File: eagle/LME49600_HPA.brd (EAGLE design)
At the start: 93.7 x 71.1 mm, 41 parts, among them IC1 OPA2134P, IC2 OPA2134P

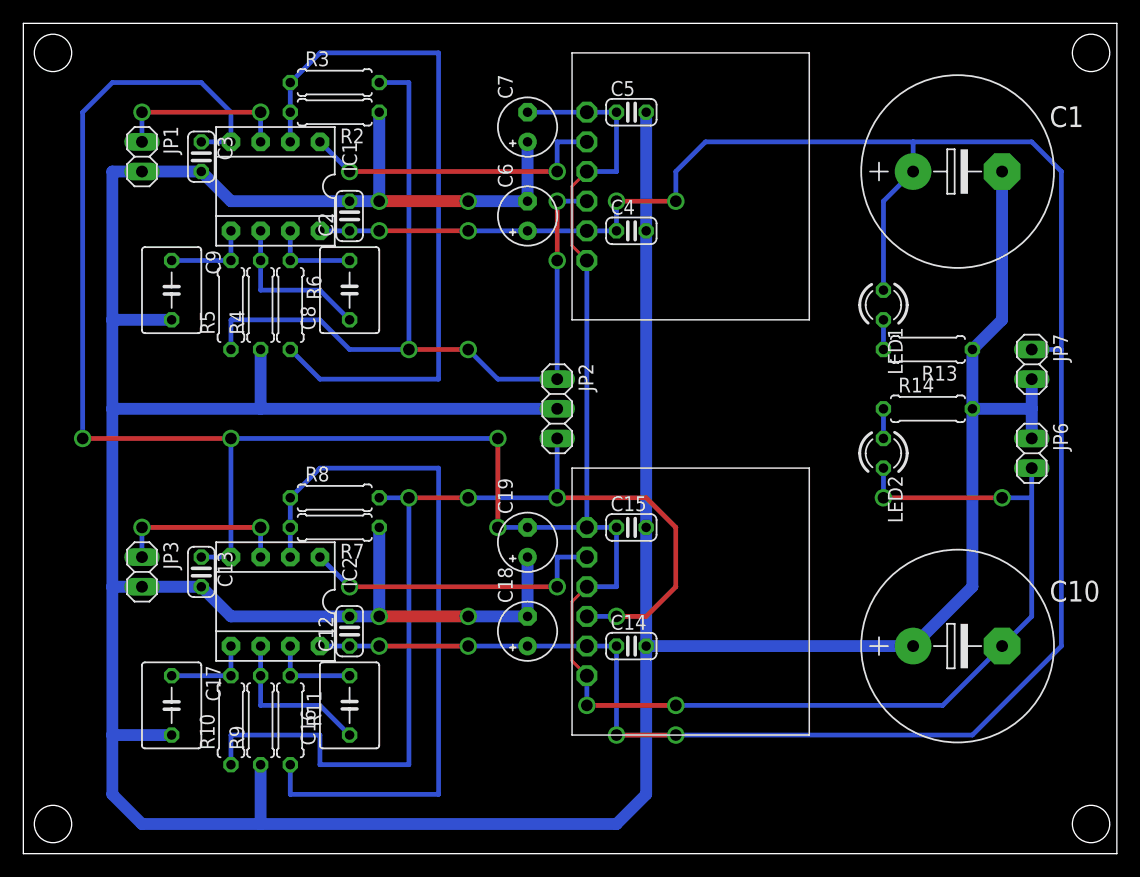
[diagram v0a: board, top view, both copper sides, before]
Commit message: Update: the board design (tantal->Alminium)
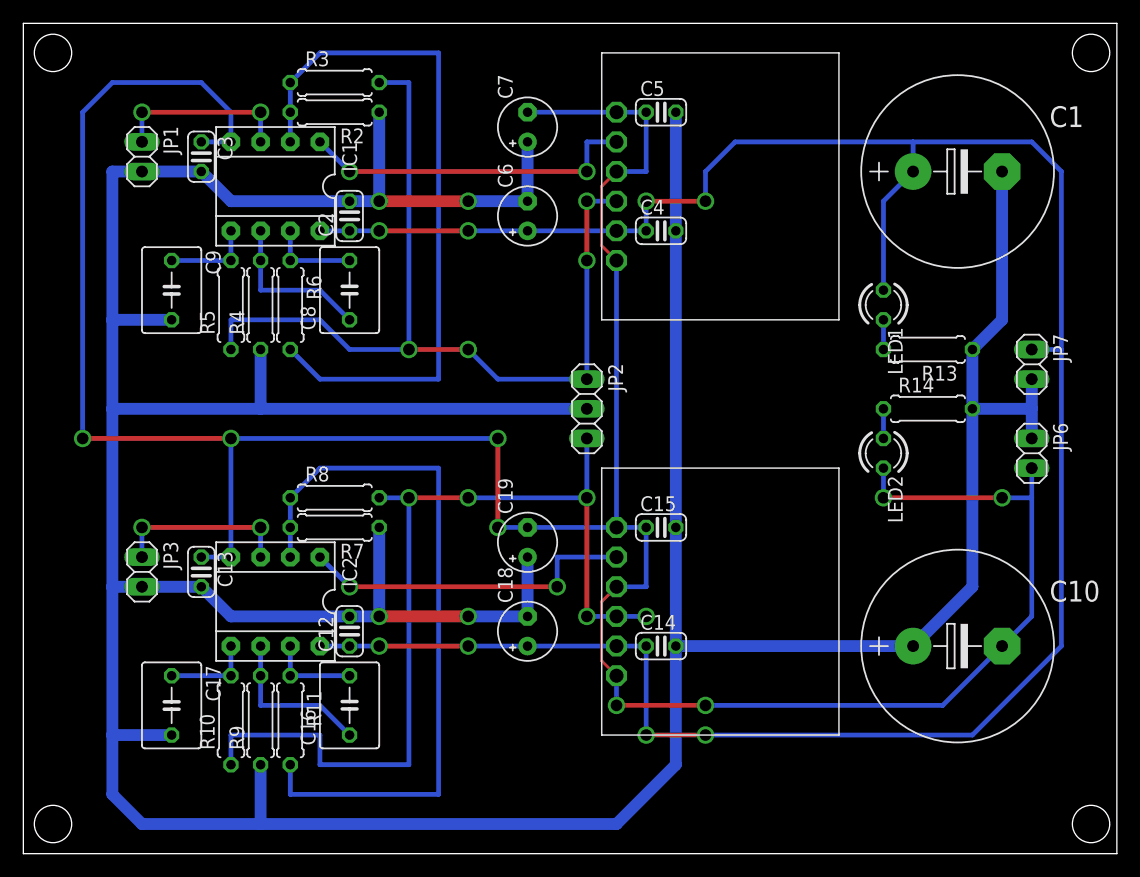
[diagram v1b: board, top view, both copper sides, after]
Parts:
- moved C14 2.54 mm to (54.6, 17.8)
- moved C15 2.54 mm to (54.6, 27.9)
- moved C4 2.54 mm to (54.6, 53.3)
- moved C5 2.54 mm to (54.6, 63.5)
- moved JP2 2.54 mm to (48.3, 38.1)
- moved U$1 2.54 mm to (59.7, 57.1)
- moved U$2 2.54 mm to (59.7, 21.6)
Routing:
- net N$13: track 88.5 -> 81.3 mm, vias 4 -> 5
- net V-: track 248.7 -> 251.2 mm
- net N$7: track 26.5 -> 29.0 mm
- net N$5: track 26.5 -> 29.0 mm
- net N$14: track 75.8 -> 78.3 mm
- net AGND: track 396.0 -> 397.0 mm

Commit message: Update: Eagle files
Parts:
- C18, C19, C6, C7: value 4.7uF -> 10uF
- R11, R2, R3, R6, R7, R8: value 1.2k -> 1k
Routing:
- net N$13: track 81.3 -> 78.7 mm, vias 5 -> 4
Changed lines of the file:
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@@
 </element>
 <element name="JP1" library="pinhead" package="1X02" value="IN" x="10.16" y="59.69" rot="R270"/>
-<element name="R2" library="rcl" package="0207/7" value="1.2k" x="26.67" y="63.5" rot="R180"/>
-<element name="R3" library="rcl" package="0207/7" value="1.2k" x="26.67" y="66.04"/>
+<element name="R2" library="rcl" package="0207/7" value="1k" x="26.67" y="63.5" rot="R180"/>
+<element name="R3" library="rcl" package="0207/7" value="1k" x="26.67" y="66.04"/>
 <element name="R4" library="rcl" package="0207/7" value="1M" x="20.32" y="46.99" rot="R90"/>
 <element name="R5" library="rcl" package="0207/7" value="1M" x="17.78" y="46.99" rot="R90"/>
 <element name="C8" library="rcl" package="C050-050X075" value="1.0uF" x="27.94" y="48.26" rot="R90"/>
 <element name="C9" library="rcl" package="C050-050X075" value="1.0uF" x="12.7" y="48.26" rot="R270"/>
-<element name="R6" library="rcl" package="0207/7" value="1.2k" x="22.86" y="46.99" rot="R270"/>
+<element name="R6" library="rcl" package="0207/7" value="1k" x="22.86" y="46.99" rot="R270"/>
 <element name="C1" library="rcl" package="E7,5-16" value="470uF" x="80.01" y="58.42"/>
 <element name="C10" library="rcl" package="E7,5-16" value="470uF" x="80.01" y="17.78"/>
-<element name="C6" library="rcl" package="E2,5-5" value="4.7uF" x="43.18" y="54.61" rot="R90"/>
-<element name="C7" library="rcl" package="E2,5-5" value="4.7uF" x="43.18" y="62.23" rot="R90"/>
+<element name="C6" library="rcl" package="E2,5-5" value="10uF" x="43.18" y="54.61" rot="R90"/>
+<element name="C7" library="rcl" package="E2,5-5" value="10uF" x="43.18" y="62.23" rot="R90"/>
 <element name="JP3" library="pinhead" package="1X02" value="IN" x="10.16" y="24.13" rot="R270"/>
 <element name="IC2" library="burr-brown" package="DIL08" value="OPA2134P" x="21.59" y="21.59" rot="R180">
@@
 <attribute name="OC_FARNELL" value="1097574" x="21.59" y="16.51" size="1.778" layer="27" rot="R180" display="off"/>
 </element>
-<element name="R7" library="rcl" package="0207/7" value="1.2k" x="26.67" y="27.94" rot="R180"/>
+<element name="R7" library="rcl" package="0207/7" value="1k" x="26.67" y="27.94" rot="R180"/>
 <element name="C12" library="rcl" package="C025-024X044" value="0.1uF" x="27.94" y="19.05" rot="R90"/>
 <element name="C13" library="rcl" package="C025-024X044" value="0.1uF" x="15.24" y="24.13" rot="R270"/>
-<element name="R8" library="rcl" package="0207/7" value="1.2k" x="26.67" y="30.48"/>
+<element name="R8" library="rcl" package="0207/7" value="1k" x="26.67" y="30.48"/>
 <element name="C14" library="rcl" package="C025-024X044" value="0.1uF" x="54.61" y="17.78"/>
 <element name="C15" library="rcl" package="C025-024X044" value="0.1uF" x="54.61" y="27.94"/>
@@
 <element name="C16" library="rcl" package="C050-050X075" value="1.0uF" x="27.94" y="12.7" rot="R90"/>
 <element name="C17" library="rcl" package="C050-050X075" value="1.0uF" x="12.7" y="12.7" rot="R270"/>
-<element name="R11" library="rcl" package="0207/7" value="1.2k" x="22.86" y="11.43" rot="R270"/>
-<element name="C18" library="rcl" package="E2,5-5" value="4.7uF" x="43.18" y="19.05" rot="R90"/>
-<element name="C19" library="rcl" package="E2,5-5" value="4.7uF" x="43.18" y="26.67" rot="R90"/>
+<element name="R11" library="rcl" package="0207/7" value="1k" x="22.86" y="11.43" rot="R270"/>
+<element name="C18" library="rcl" package="E2,5-5" value="10uF" x="43.18" y="19.05" rot="R90"/>
+<element name="C19" library="rcl" package="E2,5-5" value="10uF" x="43.18" y="26.67" rot="R90"/>
 <element name="U$1" library="mylib2" package="TO-263-5L" value="LME49600-BRD3" x="59.69" y="57.15" rot="R270"/>
 <element name="U$2" library="mylib2" package="TO-263-5L" value="LME49600-BRD3" x="59.69" y="21.59" rot="R270"/>
@@
 <via x="38.1" y="30.48" extent="1-16" drill="1" shape="square"/>
 <via x="33.02" y="30.48" extent="1-16" drill="1" shape="square"/>
-<wire x1="50.8" y1="20.32" x2="53.34" y2="20.32" width="0.4064" layer="16"/>
-<via x="53.34" y="20.32" extent="1-16" drill="1" shape="square"/>
 <via x="48.26" y="30.48" extent="1-16" drill="1" shape="square"/>
 <wire x1="48.26" y1="35.56" x2="48.26" y2="30.48" width="0.4064" layer="16"/>
 <wire x1="25.4" y1="7.62" x2="33.02" y2="7.62" width="0.4064" layer="16"/>
 <wire x1="33.02" y1="7.62" x2="33.02" y2="30.48" width="0.4064" layer="16"/>
-<wire x1="50.8" y1="20.32" x2="48.26" y2="20.32" width="0.4064" layer="16"/>
 <wire x1="48.26" y1="20.32" x2="48.26" y2="30.48" width="0.4064" layer="1"/>
 <via x="48.26" y="20.32" extent="1-16" drill="1" shape="square"/>
+<wire x1="48.26" y1="20.32" x2="50.8" y2="20.32" width="0.4064" layer="16"/>
 </signal>
 <signal name="N$15">

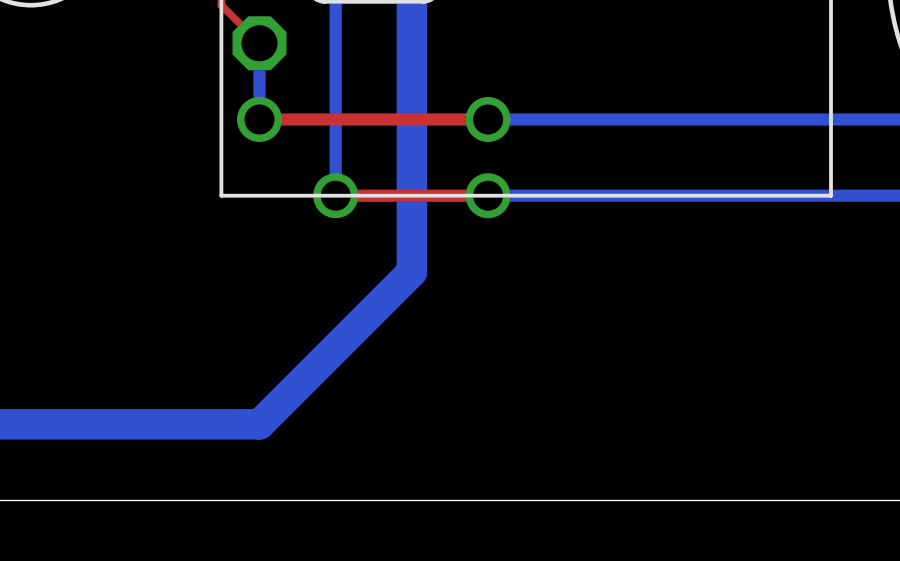
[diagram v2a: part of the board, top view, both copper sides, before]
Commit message: Eagle Files: Add TP-GND
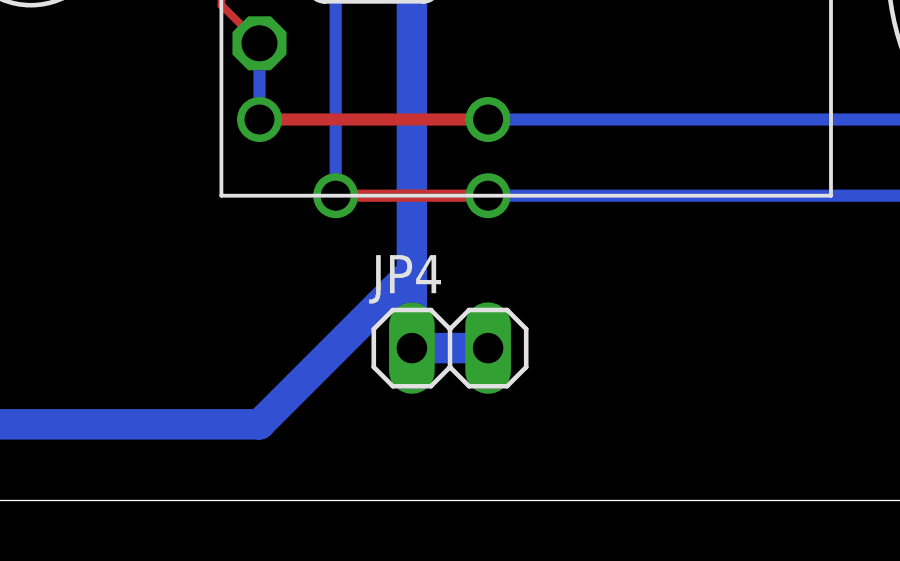
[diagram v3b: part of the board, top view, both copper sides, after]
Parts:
- added JP4: TP_GND, pinhead:1X02
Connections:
- net AGND: now also JP4.1, JP4.2
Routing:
- net AGND: track 397.0 -> 402.1 mm
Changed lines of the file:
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@@
 <element name="JP6" library="pinhead" package="1X02" value="PWR-" x="86.36" y="34.29" rot="R270"/>
 <element name="JP2" library="pinhead" package="1X03" value="OUT" x="48.26" y="38.1" rot="R270"/>
+<element name="JP4" library="pinhead" package="1X02" value="TP_GND" x="57.15" y="5.08"/>
 </elements>
 <signals>
@@
 <wire x1="83.82" y1="45.72" x2="81.28" y2="43.18" width="1.016" layer="16"/>
 <wire x1="81.28" y1="22.86" x2="81.28" y2="38.1" width="1.016" layer="16"/>
+<contactref element="JP4" pad="1"/>
+<contactref element="JP4" pad="2"/>
+<wire x1="55.88" y1="5.08" x2="55.88" y2="7.62" width="1.016" layer="16"/>
+<wire x1="55.88" y1="5.08" x2="58.42" y2="5.08" width="1.016" layer="16"/>
 </signal>
 <signal name="N$3">

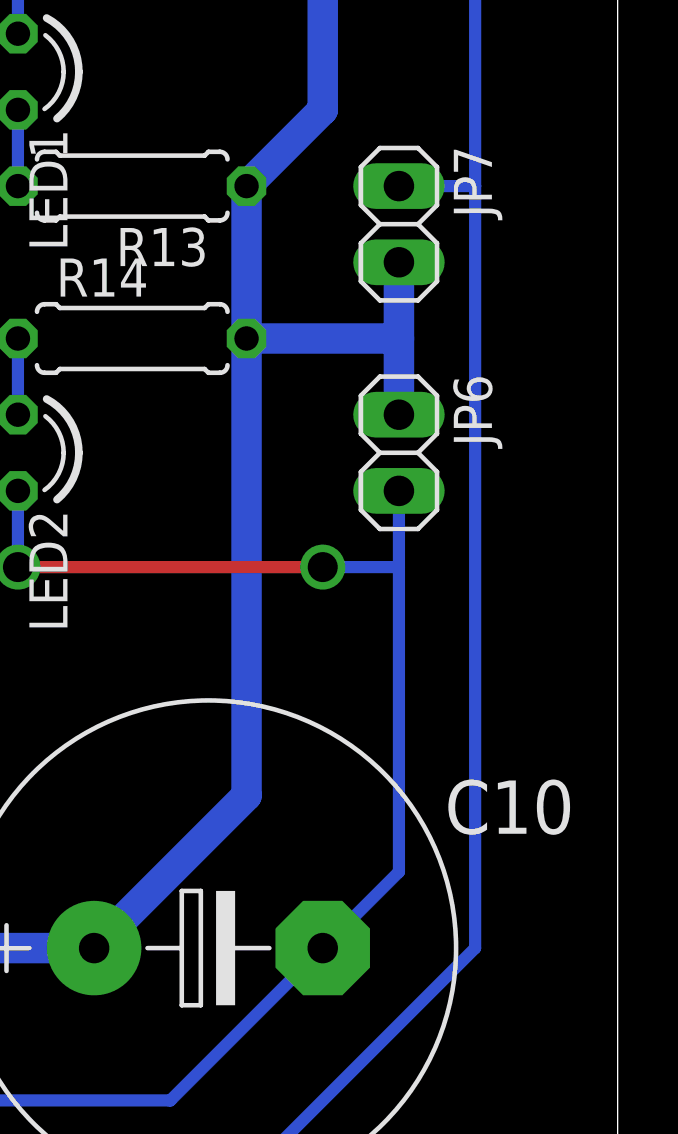
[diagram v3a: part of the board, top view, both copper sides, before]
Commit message: Add: PWR LED
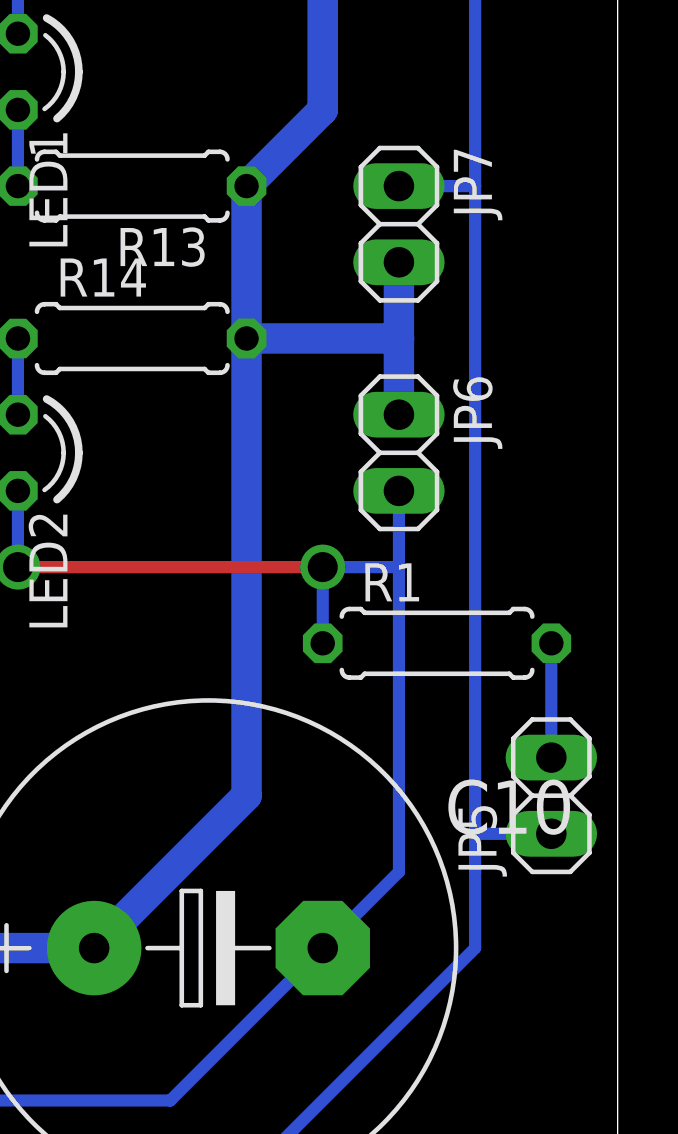
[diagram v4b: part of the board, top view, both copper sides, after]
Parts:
- added JP5: PWR_LED, pinhead:1X02
- added R1: 3.3k, rcl:0207/7
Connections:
- new net N$16: JP5.2, R1.2
- net V+: now also JP5.1
- net V-: now also R1.1
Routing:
- net N$16: track 0.00 -> 3.81 mm
- net V+: track 201.9 -> 204.4 mm
- net V-: track 251.2 -> 253.7 mm
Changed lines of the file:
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@@
 <element name="JP2" library="pinhead" package="1X03" value="OUT" x="48.26" y="38.1" rot="R270"/>
 <element name="JP4" library="pinhead" package="1X02" value="TP_GND" x="57.15" y="5.08"/>
+<element name="R1" library="rcl" package="0207/7" value="3.3k" x="87.63" y="27.94"/>
+<element name="JP5" library="pinhead" package="1X02" value="PWR_LED" x="91.44" y="22.86" rot="R90"/>
 </elements>
 <signals>
@@
 <wire x1="83.82" y1="30.48" x2="86.36" y2="30.48" width="0.4064" layer="16"/>
 <wire x1="83.82" y1="17.78" x2="78.74" y2="12.7" width="0.4064" layer="16"/>
+<contactref element="R1" pad="1"/>
+<wire x1="83.82" y1="30.48" x2="83.82" y2="27.94" width="0.4064" layer="16"/>
 </signal>
 <signal name="V+">
@@
 <via x="53.34" y="55.88" extent="1-16" drill="1" shape="square"/>
 <via x="58.42" y="55.88" extent="1-16" drill="1" shape="square"/>
-<wire x1="88.9" y1="17.78" x2="88.9" y2="43.18" width="0.4064" layer="16"/>
+<wire x1="88.9" y1="17.78" x2="88.9" y2="20.32" width="0.4064" layer="16"/>
+<wire x1="88.9" y1="21.59" x2="88.9" y2="43.18" width="0.4064" layer="16"/>
 <wire x1="88.9" y1="43.18" x2="88.9" y2="58.42" width="0.4064" layer="16"/>
 <wire x1="88.9" y1="58.42" x2="86.36" y2="60.96" width="0.4064" layer="16"/>
@@
 <wire x1="73.66" y1="55.88" x2="76.2" y2="58.42" width="0.4064" layer="16"/>
 <wire x1="53.34" y1="10.16" x2="58.42" y2="10.16" width="0.4064" layer="1"/>
+<contactref element="JP5" pad="1"/>
+<wire x1="91.44" y1="21.59" x2="88.9" y2="21.59" width="0.4064" layer="16"/>
+<wire x1="88.9" y1="21.59" x2="88.9" y2="20.32" width="0.4064" layer="16"/>
 </signal>
 <signal name="N$6">
@@
 <wire x1="73.66" y1="38.1" x2="73.66" y2="35.56" width="0.4064" layer="16"/>
 </signal>
+<signal name="N$16">
+<contactref element="R1" pad="2"/>
+<contactref element="JP5" pad="2"/>
+<wire x1="91.44" y1="27.94" x2="91.44" y2="24.13" width="0.4064" layer="16"/>
+</signal>
 </signals>
+<errors>
+</errors>
 </board>
 </drawing>
